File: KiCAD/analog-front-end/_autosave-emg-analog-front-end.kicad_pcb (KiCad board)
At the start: 2 copper layers, 42 x 20 mm, 41 parts, among them J1 Conn_01x03, J2 Conn_01x04_Female, J3 Conn_01x04_Female, U1 LMC6482, U2 AD620, U3 AD8619ARUZ-REEL

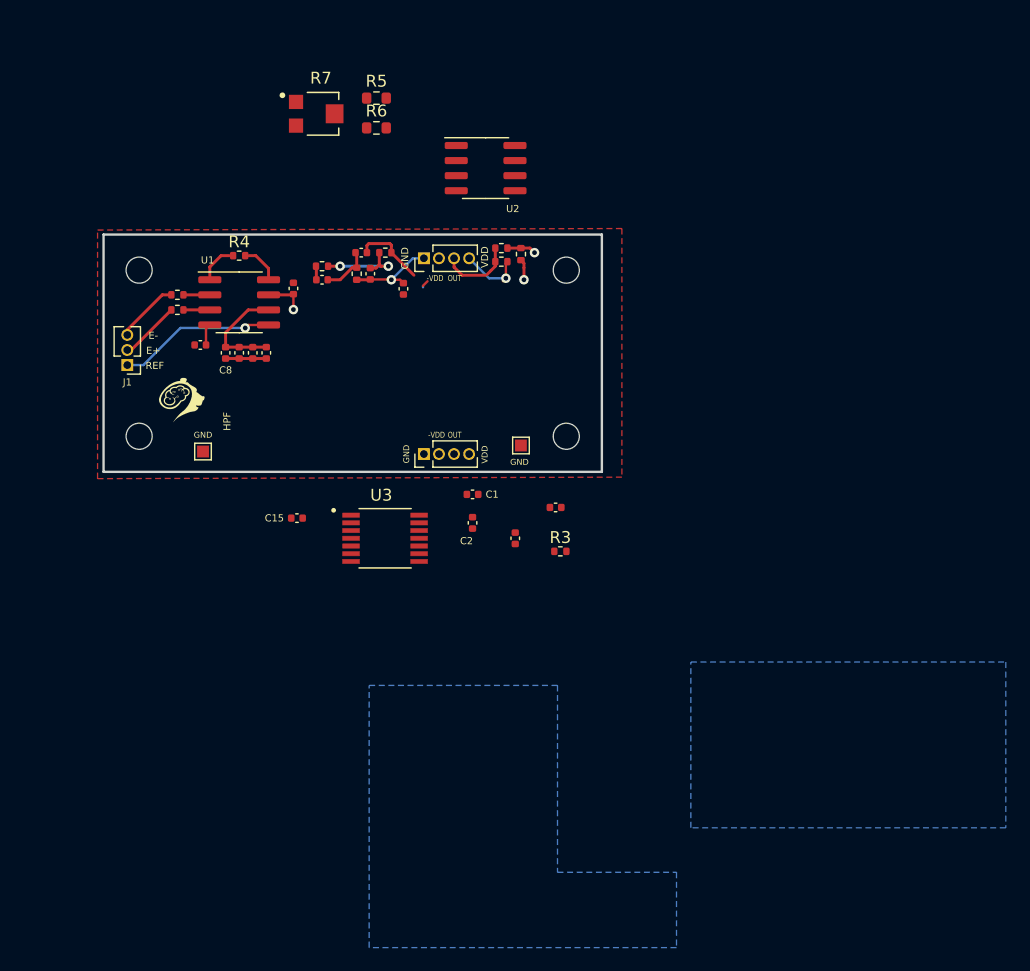
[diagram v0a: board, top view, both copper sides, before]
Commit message: modifying the pcb for new electrode placement and replacing op amps
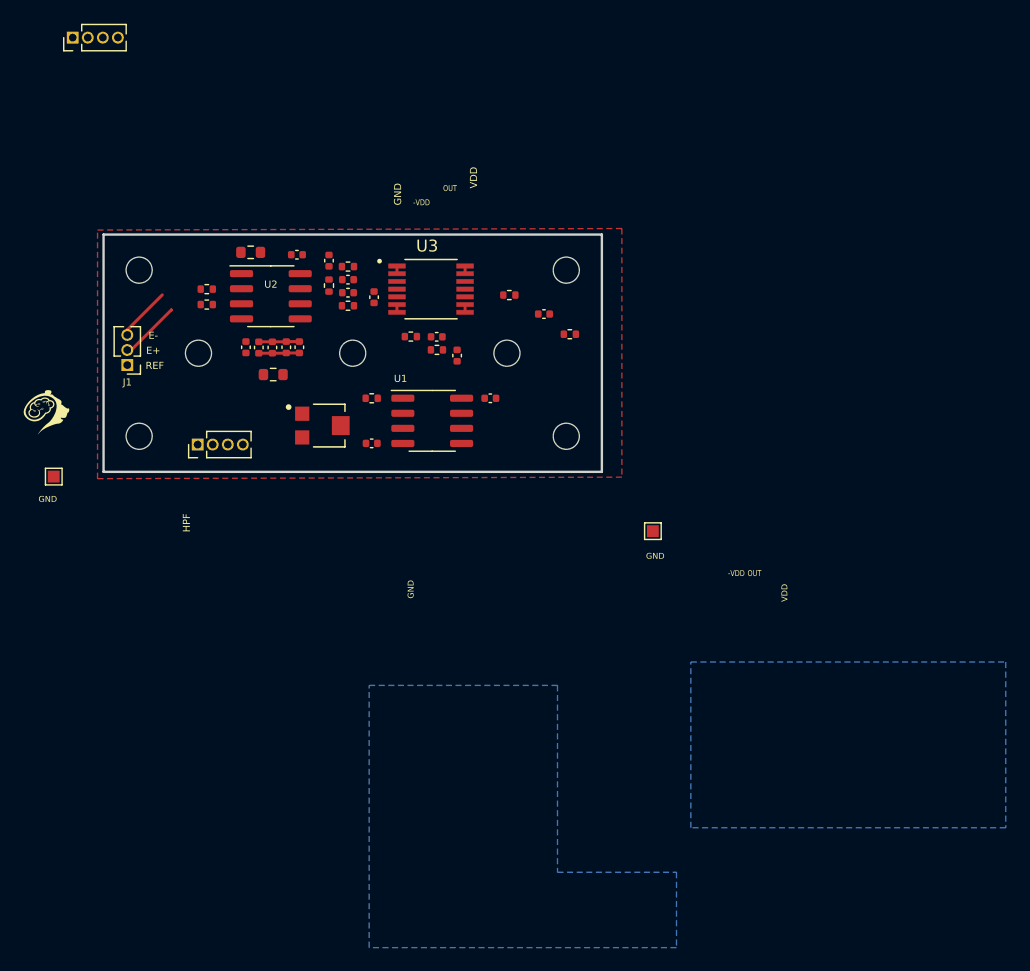
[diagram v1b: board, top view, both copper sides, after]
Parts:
- added H1: MountingHole, MountingHole:MountingHole_2.2mm_M2, F.Cu at (8.00, 10.0)
- added H1: MountingHole, MountingHole:MountingHole_2.2mm_M2, F.Cu at (34.0, 10.0)
- added H1: MountingHole, MountingHole:MountingHole_2.2mm_M2, F.Cu at (21.0, 10.0)
- moved J2 35.0 mm to (-2.60, -16.6)
- moved R7 26.3 mm to (18.5, 16.1)
- moved C13 26.0 mm to (20.6, 3.80), turned to 180 degrees
- moved C12 23.4 mm to (22.8, 5.28), turned to 90 degrees
- moved R6 22.5 mm to (14.3, 11.8)
- moved R3 22.1 mm to (25.9, 8.60), turned to 180 degrees
- moved C3 21.7 mm to (29.8, 10.2), turned to 90 degrees
- moved U3 21.4 mm to (27.6, 4.60)
- moved U2 21.1 mm to (14.1, 5.20)
- moved C15 19.5 mm to (20.6, 4.90), turned to 0 degrees
- moved U1 19.1 mm to (27.7, 15.7)
- moved J3 19.1 mm to (7.93, 17.7)
- moved R4 18.5 mm to (28.1, 9.72), turned to 180 degrees
- moved R8 17.5 mm to (22.6, 13.8), turned to 180 degrees
- moved R5 16.8 mm to (12.4, 1.50)
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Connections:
- C11 pad 1: unconnected-(C11-Pad1) -> -VDD
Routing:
- net AOUT: track 14.0 -> 0.00 mm, vias 2 -> 0
- net unconnected-(U1-Pad5): track 13.4 -> 0.00 mm, vias 1 -> 0
- net VDD: track 9.60 -> 0.00 mm, vias 1 -> 0
- net GND: track 7.67 -> 0.07 mm, vias 1 -> 0
- net /HPF_IN: track 10.1 -> 3.42 mm
- net NOTCH_OUT: track 6.11 -> 0.00 mm
- net E-: track 10.5 -> 4.60 mm
- net LPF_OUT: track 5.86 -> 0.65 mm, vias 2 -> 0
- net E+: track 0.00 -> 5.11 mm
- net Net-(C13-Pad2): track 4.17 -> 0.00 mm
- net /AMP_OUT: track 3.12 -> 0.00 mm
- net -VDD: track 2.72 -> 0.00 mm
- net Net-(R7-Pad1): track 2.22 -> 0.00 mm
- net Net-(R7-Pad2): track 1.75 -> 0.00 mm, vias 1 -> 0
- net AMP_IN: track 2.22 -> 0.65 mm
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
